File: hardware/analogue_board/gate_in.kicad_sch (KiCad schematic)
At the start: 46 parts, among them J801 Gate in holes, J802 Probe holes: PR1-10 100 kΩ, P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, U801 LM393DR2G, U802 LM393DR2G

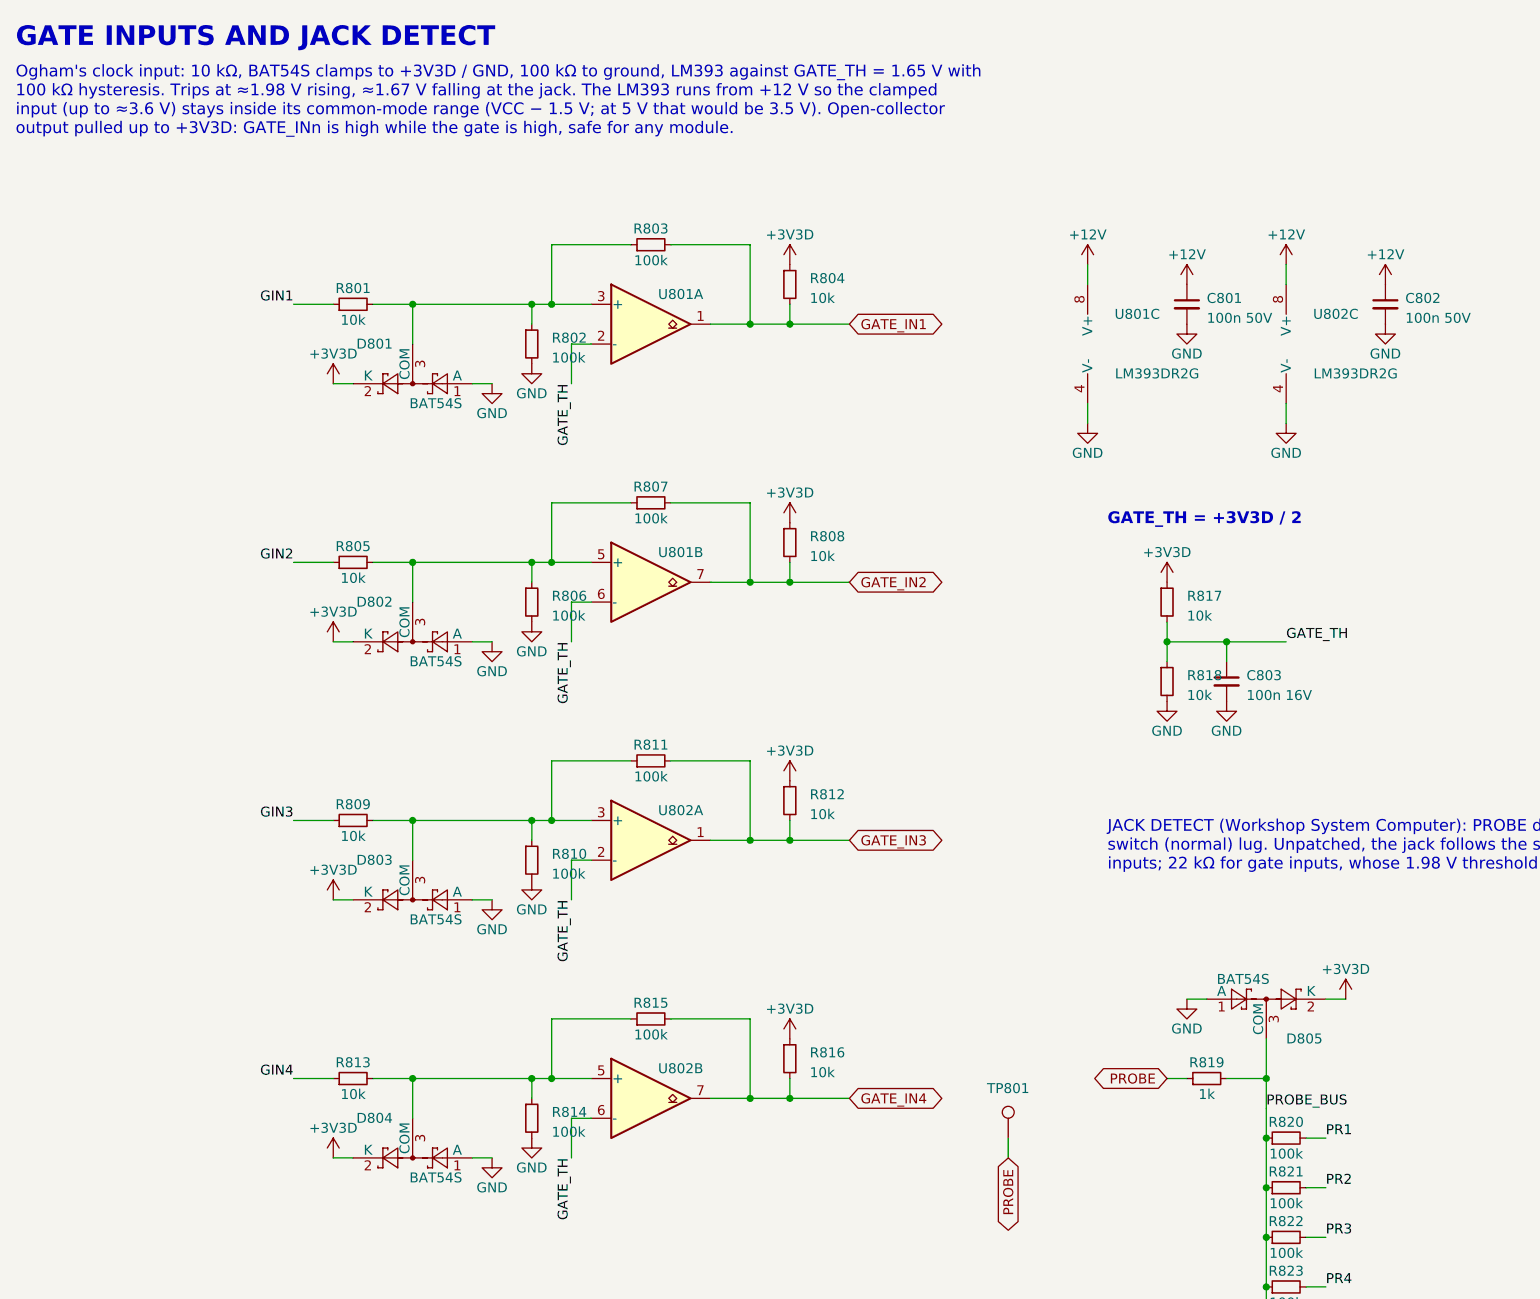
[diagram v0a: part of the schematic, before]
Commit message: Analogue board: block review applied, TRS MIDI, ESP32-P4 support
Checkpoint 1 schematic rebuilt after a block-by-block prior-art review
(docs/analogue_board_review/, seven reports and an index).

Schematic:
- Codec: 20 Vpp in and out (15k input feedback; balanced MFB output,
  gain 2.5, 1 nF C0G); ferrite and 5.1 ohm on the codec supplies; VCOM
  decoupled at each input; CODEC_RST to a hole.
- Power: 680 ohm minimum load on +3V3D; buck input ferrite and EN
  divider; SS34 at D201-D203; Q201/JP201 MOD_5V bypass for the ESP32-P4.
- CV in: 15 V TVS at each jack, 1 nF at each ADC input, 1206 outputs.
- CV out: 12k/22k offset with 1 nF, 33k gain; CV7-8 feedback from the
  jack side of the 1k.
- Gates and panel: CS_595 pull-up, GATE_OE_N on J603, 1M wiper
  pull-downs, POT_REF, button RC order, 47 uF at the LED holes.
- New sheet 10: TRS MIDI (Type A), H11L1 in, 5 V buffered out.
- Layout: no overlapping text on any sheet.

ERC 0/0; netlist identical to intent (345 nets); 21 ICs against
datasheets; 17 Extended part types.

Spec v0.4: David's decisions (TVS yes, CV +/-5 V with a +/-10 V
variant, ESP32-P4 accommodated, power header free to move), the
corrections, and a firmware requirements list in section 15.

Co-Authored-By: Claude Opus 5.5 <noreply@anthropic.com>
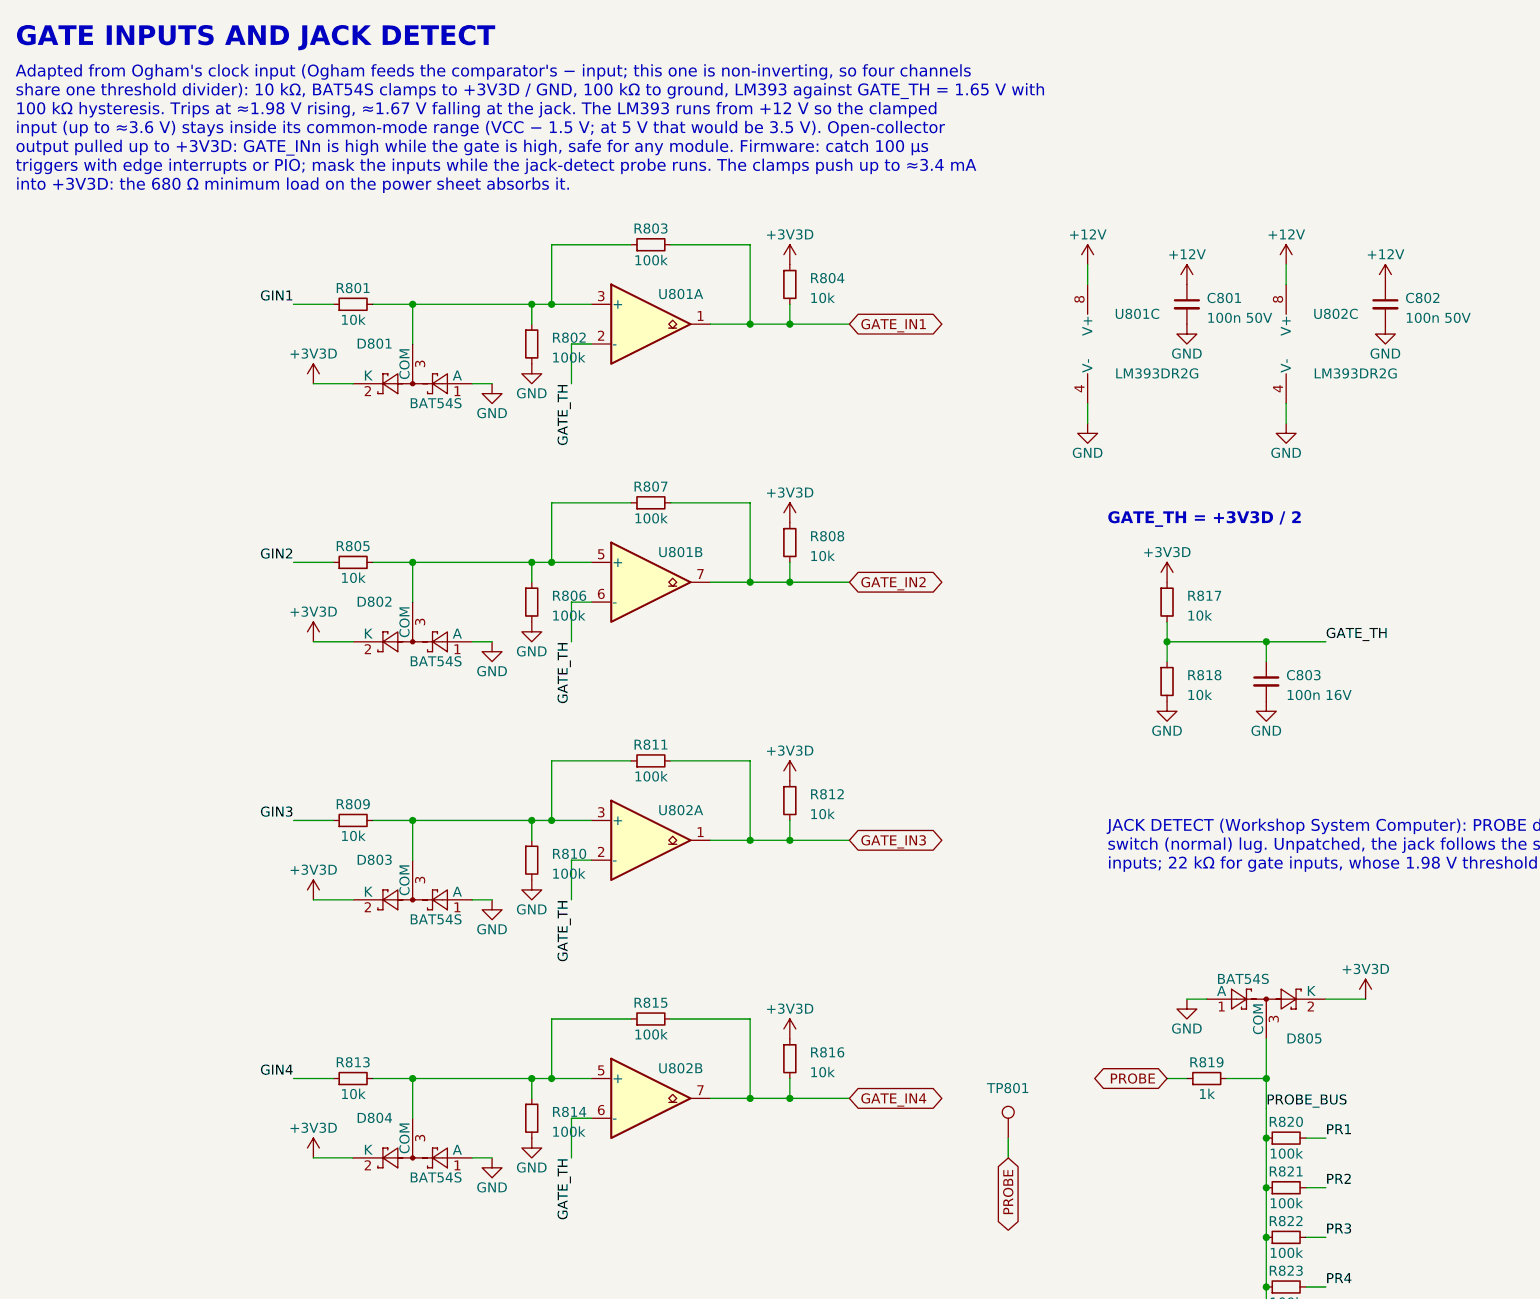
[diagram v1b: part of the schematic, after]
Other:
- note added: "Adapted from Ogham's clock input (Ogham feeds the comparator's − input; this one is non-inverting, so four channels share one threshold divider): 10 kΩ, BAT54S clamps to +3V3D / GND, 100 kΩ to ground, LM393 against GATE_TH = 1.65 V with 100 kΩ hysteresis. Trips at ≈1.98 V rising, ≈1.67 V falling at the jack. The LM393 runs from +12 V so the clamped input (up to ≈3.6 V) stays inside its common-mod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"
- note removed: "Ogham's clock input: 10 kΩ, BAT54S clamps to +3V3D / GND, 100 kΩ to ground, LM393 against GATE_TH = 1.65 V with 100 kΩ hysteresis. Trips at ≈1.98 V rising, ≈1.67 V falling at the jack. The LM393 runs from +12 V so the clamped input (up to ≈3.6 V) stays inside its common-mode range (VCC − 1.5 V; at 5 V that would be 3.5 V). Open-collector output pulled up to +3V3D: GATE_INn is high while the gate 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"
- moved on the sheet: C803

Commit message: Analogue board: checkpoint 3 started; double-sided, floorplan placed
- pcb.py generates analogue_board.kicad_pcb from the netlist: outline,
  JLC 4-layer stack-up, every footprint with nets and schematic links
  (KiCad schematic parity: 0 differences), parked parts beside the board,
  courtyard area budget, DRC and 3D renders of both faces.
- Area budget: the courtyards need 104% of one face before routing, so
  David chose double-sided assembly (JLC Standard PCBA, about $100 more
  per order, to confirm on a quote).
- Floorplan in placement.py: analogue ICs at the top under the modules,
  furthest from the buck; logic below; power bottom right around J201;
  MIDI bottom left; 99 wiring-field holes in three columns lined up with
  the edge-strip positions, each group beside its circuit.
- Library: module socket courtyards cover only their header rows; the
  wiring holes get their own footprint with a one-pitch courtyard.
- Spec records the decision, the floorplan and David's answers: 11 mm to
  the deck in 10HP (deck parts 2 mm at most); holes tinned both faces.

Co-Authored-By: Claude Opus 5.5 <noreply@anthropic.com>
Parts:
- J801: footprint Connector_PinHeader_2.54mm:PinHeader_1x05_P2.54mm_Vertical -> analogue_board:WiringHoles_1x05
- J802: footprint Connector_PinHeader_2.54mm:PinHeader_1x14_P2.54mm_Vertical -> analogue_board:WiringHoles_1x14
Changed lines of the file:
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@@
 			)
 		)
-		(property "Footprint" "Connector_PinHeader_2.54mm:PinHeader_1x05_P2.54mm_Vertical"
+		(property "Footprint" "analogue_board:WiringHoles_1x05"
 			(at 279.4 66.04 0)
 			(effects
@@
 			)
 		)
-		(property "Footprint" "Connector_PinHeader_2.54mm:PinHeader_1x14_P2.54mm_Vertical"
+		(property "Footprint" "analogue_board:WiringHoles_1x14"
 			(at 243.84 203.2 0)
 			(effects
